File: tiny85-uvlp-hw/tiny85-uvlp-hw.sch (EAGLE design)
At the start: 10 parts, among them J1 AVR_SPI, Q1 NFET, U1 TINY85-20-DIP

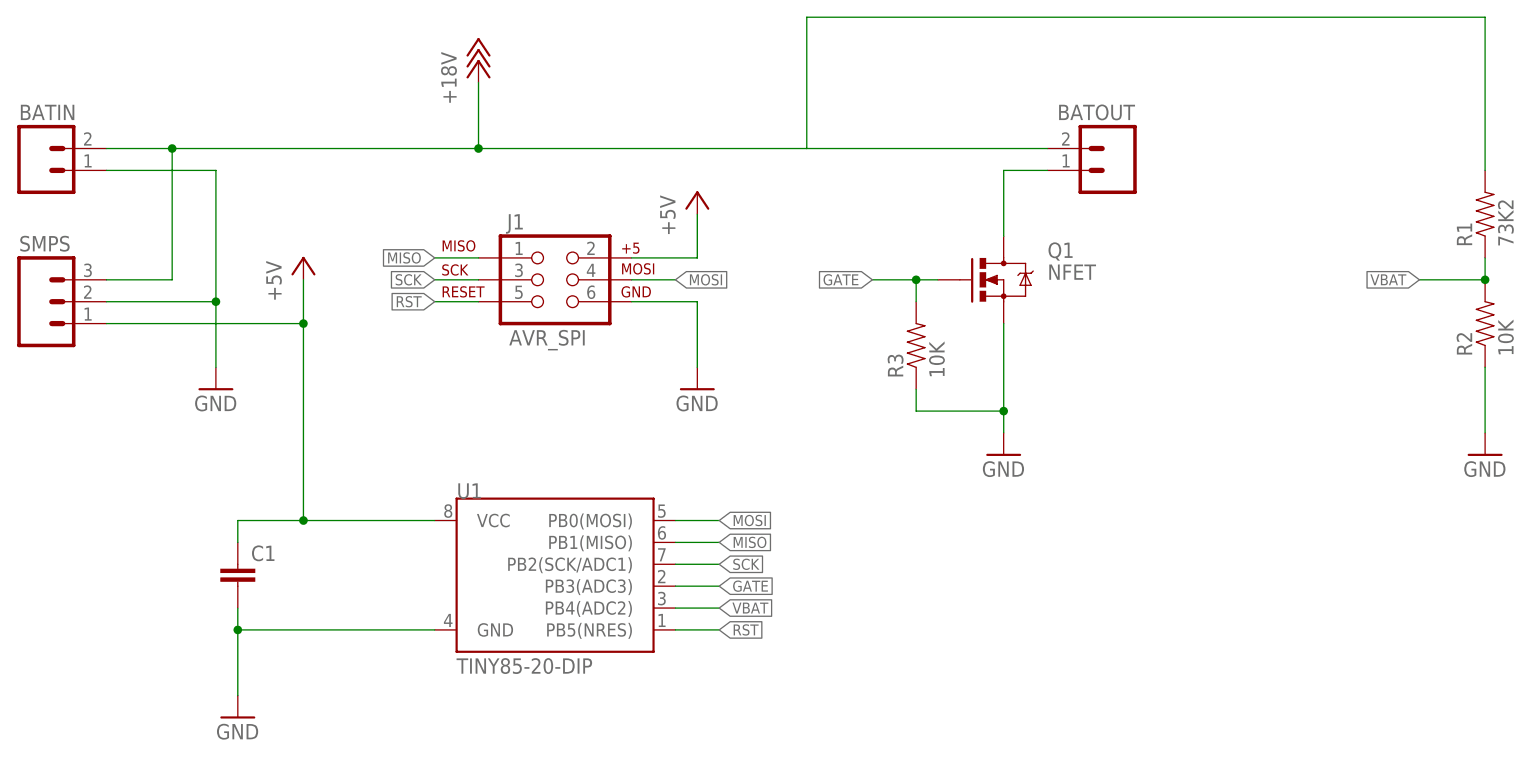
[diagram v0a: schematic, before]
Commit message: fine tune schematic and routing
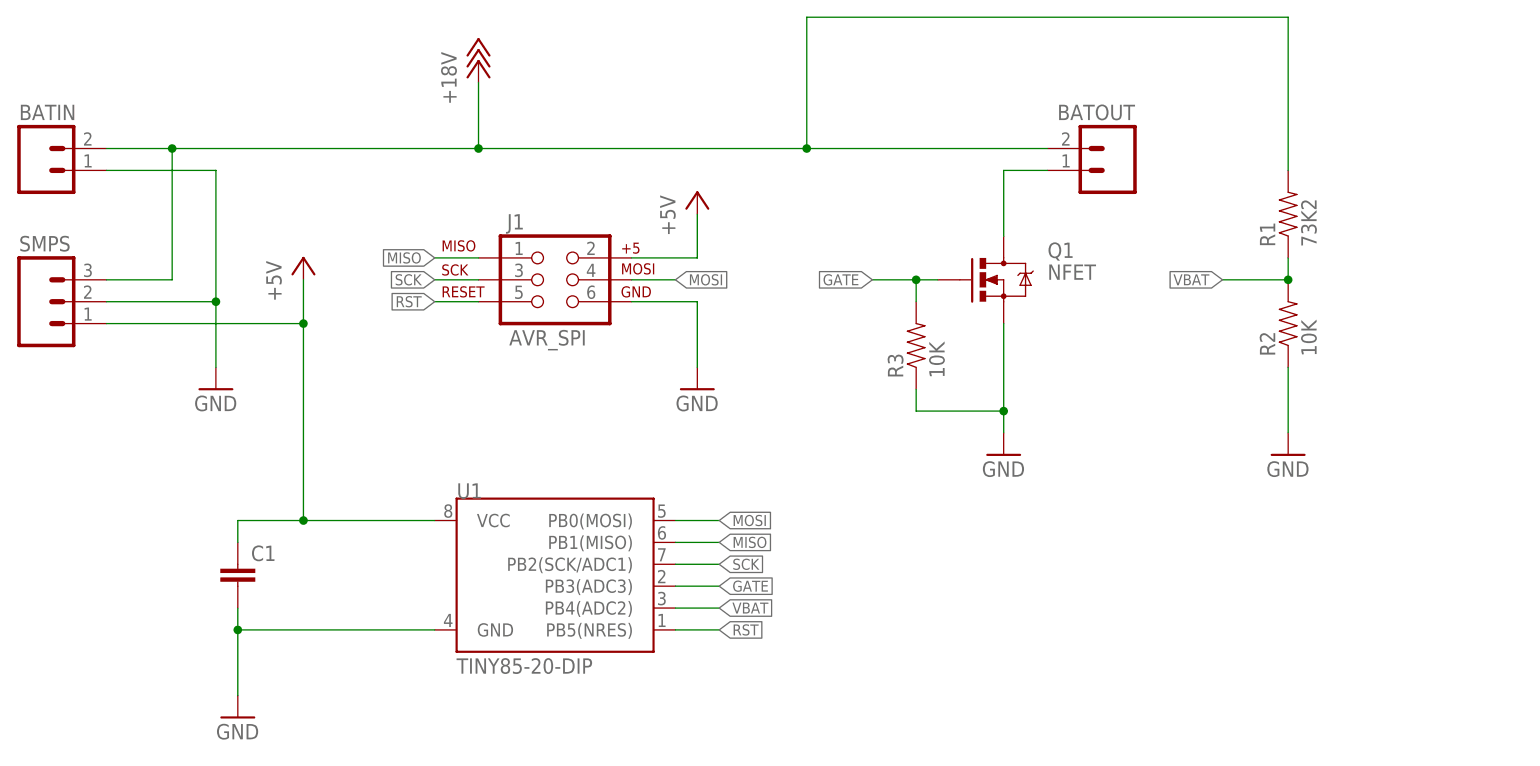
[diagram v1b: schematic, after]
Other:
- moved on the sheet: R1, R2
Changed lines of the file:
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@@
 <instance part="P+3" gate="1" x="86.36" y="109.22"/>
 <instance part="GND3" gate="1" x="86.36" y="86.36"/>
-<instance part="R1" gate="G$1" x="177.8" y="106.68" rot="R90"/>
-<instance part="R2" gate="G$1" x="177.8" y="93.98" rot="R90"/>
-<instance part="GND4" gate="1" x="177.8" y="78.74"/>
+<instance part="R1" gate="G$1" x="154.94" y="106.68" rot="R90"/>
+<instance part="R2" gate="G$1" x="154.94" y="93.98" rot="R90"/>
+<instance part="GND4" gate="1" x="154.94" y="78.74"/>
 <instance part="GND5" gate="1" x="121.92" y="78.74"/>
 <instance part="R3" gate="G$1" x="111.76" y="91.44" rot="R90"/>
@@
 <junction x="25.4" y="114.3"/>
 <wire x1="99.06" y1="114.3" x2="99.06" y2="129.54" width="0.1524" layer="91"/>
-<wire x1="99.06" y1="129.54" x2="177.8" y2="129.54" width="0.1524" layer="91"/>
-<wire x1="177.8" y1="129.54" x2="177.8" y2="111.76" width="0.1524" layer="91"/>
+<wire x1="99.06" y1="129.54" x2="154.94" y2="129.54" width="0.1524" layer="91"/>
+<wire x1="154.94" y1="129.54" x2="154.94" y2="111.76" width="0.1524" layer="91"/>
 <pinref part="R1" gate="G$1" pin="2"/>
 <pinref part="SMPS" gate="J$1" pin="3"/>
+<junction x="99.06" y="114.3"/>
 </segment>
 </net>
@@
 <pinref part="R2" gate="G$1" pin="1"/>
 <pinref part="GND4" gate="1" pin="GND"/>
-<wire x1="177.8" y1="88.9" x2="177.8" y2="81.28" width="0.1524" layer="91"/>
+<wire x1="154.94" y1="88.9" x2="154.94" y2="81.28" width="0.1524" layer="91"/>
 </segment>
 <segment>
@@
 <pinref part="R2" gate="G$1" pin="2"/>
 <pinref part="R1" gate="G$1" pin="1"/>
-<wire x1="177.8" y1="99.06" x2="177.8" y2="101.6" width="0.1524" layer="91"/>
-<wire x1="177.8" y1="99.06" x2="170.18" y2="99.06" width="0.1524" layer="91"/>
-<junction x="177.8" y="99.06"/>
-<label x="170.18" y="99.06" size="1.27" layer="95" rot="R180" xref="yes"/>
+<wire x1="154.94" y1="99.06" x2="154.94" y2="101.6" width="0.1524" layer="91"/>
+<wire x1="154.94" y1="99.06" x2="147.32" y2="99.06" width="0.1524" layer="91"/>
+<junction x="154.94" y="99.06"/>
+<label x="147.32" y="99.06" size="1.27" layer="95" rot="R180" xref="yes"/>
 </segment>
 <segment>
